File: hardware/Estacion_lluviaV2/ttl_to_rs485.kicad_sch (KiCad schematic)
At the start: 16 parts, among them U1 SP3485EN, U5 SP3485EN

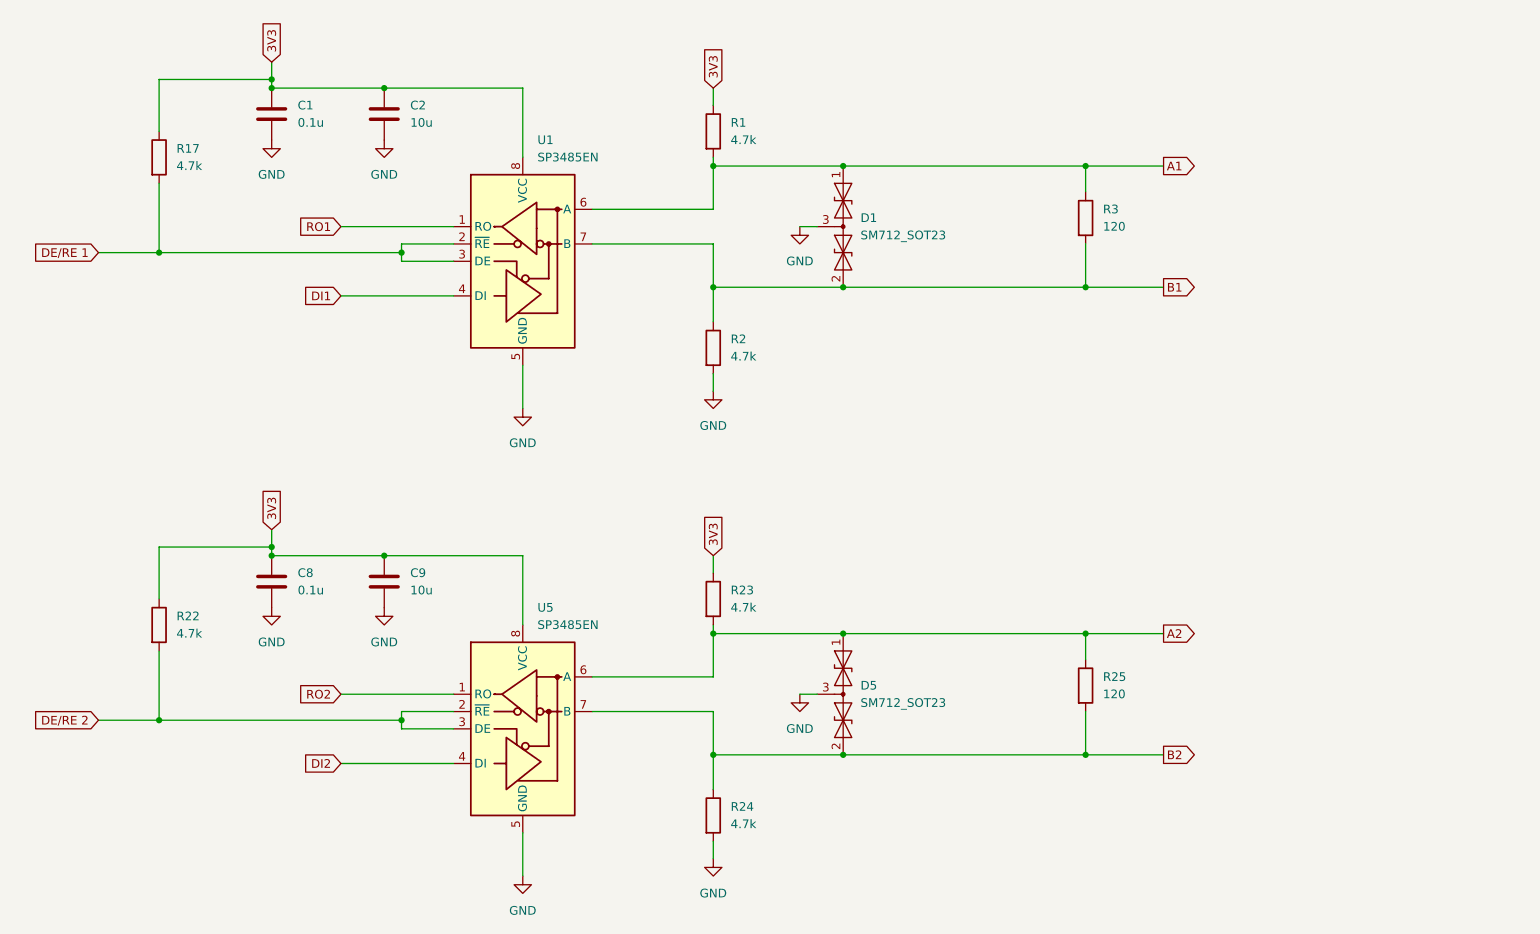
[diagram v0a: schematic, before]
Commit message: Se agregaron nuevos archivos
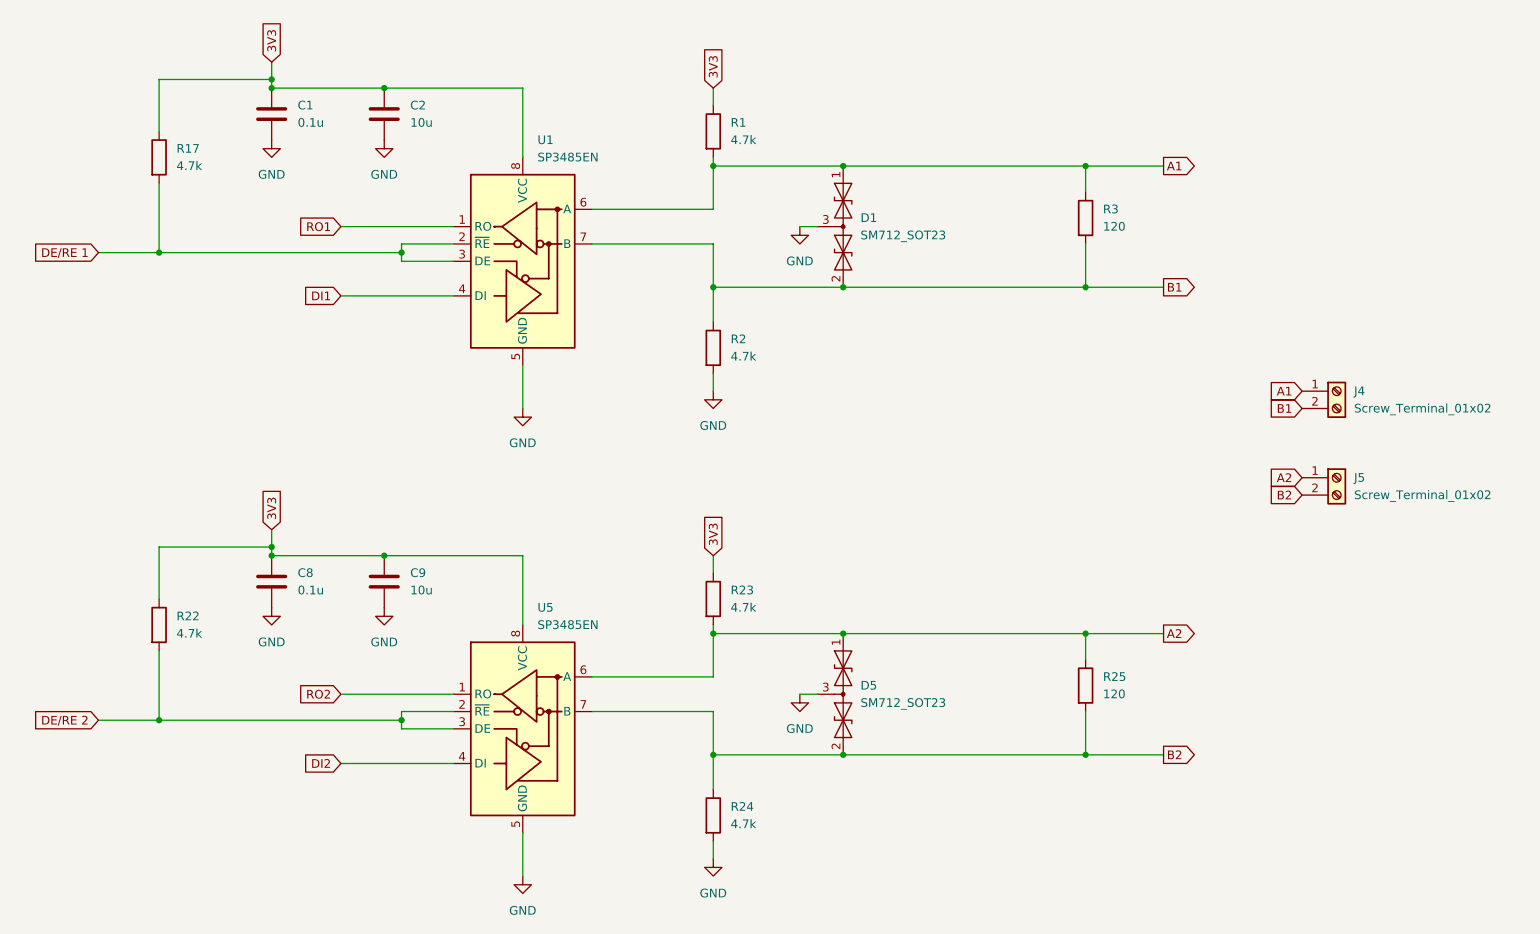
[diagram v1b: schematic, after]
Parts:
- added J4, J5: Screw_Terminal_01x02, TerminalBlock:TerminalBlock_MaiXu_MX126-5.0-02P_1x02_P5.00mm, symbol Connector:Screw_Terminal_01x02
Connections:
- net A1: now also J4.1 (Pin_1)
- net A2: now also J5.1 (Pin_1)
- net B1: now also J4.2 (Pin_2)
- net B2: now also J5.2 (Pin_2)
